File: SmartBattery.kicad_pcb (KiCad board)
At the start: 2 copper layers, 168 parts, among them J1 USB_C_Receptacle_USB2.0, J10 Conn_01x02, J11 Conn_01x02, J2 ST-USB-003A, J3 RJ45_LED_Shielded, J4 Conn_01x02, J5 Conn_01x02, J6 Conn_01x02, J7 Conn_01x02, J8 Conn_01x02, J9 Conn_01x02, Q1 AO4407A, Q10 AO4468, Q11 AO4468, Q2 2n7002K, Q3 AO4468, Q4 AO4468, Q5 AO4468, Q6 AO4468, Q7 2n7002K, Q8 AO4468, Q9 AO4468, SW1 SW_Push, SW2 SW_Push, U1 bq2477x, U2 BQ294706DSGR, U3 ITV4030, U4 BQ40Z50

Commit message: Adding lots of changes. Started output Stage
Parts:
- removed Q3, Q5: AO4468, Package_TO_SOT_SMD:TDSON-8-1
- added L2: MWSA0603-2R2MT, SmartBattery:MWSA0603, F.Cu at (16.2, 17.6)
- added U5: LM5175PWPR, SmartBattery:IC_TPS61196PWPRQ1, F.Cu at (8.07, 20.2)
- J10, J11, J4, J5, J6, J7, J8, J9: value Conn_01x02 -> JST 2P-1.0; footprint Connector_JST:JST_PH_S2B-PH-K_1x02_P2.00mm_Horizontal -> Connector_JST:JST_SH_SM02B-SRSS-TB_1x02-1MP_P1.00mm_Horizontal
- J3: value RJ45_LED_Shielded -> Barrel_Jack_MountingPin; footprint Connector_RJ:RJ45_Amphenol_RJHSE538X -> Connector_BarrelJack:BarrelJack_Horizontal
- Q10, Q11, Q4, Q6, Q8, Q9: footprint Package_TO_SOT_SMD:TDSON-8-1 -> SmartBattery:SOIC-8_Alpha_Omega
- TP18: moved to B.Cu
- moved J2 140.8 mm to (7.45, 4.47), turned to 90 degrees
- moved J1 122.3 mm to (21.8, 5.89), turned to 180 degrees
- moved D2 108.7 mm to (12.0, 52.9)
- moved D3 108.7 mm to (6.61, 52.8)
- moved D4 108.7 mm to (33.8, 53.1)
- moved D6 108.7 mm to (38.6, 53.1)
- moved D7 108.7 mm to (21.6, 52.9)
- moved J3 106.8 mm to (91.0, 11.4), turned to 180 degrees
- moved C16 104.5 mm to (75.0, 21.4)
- moved C17 104.5 mm to (65.1, 21.4)
- moved TP1 81.3 mm to (46.7, 34.4)
- moved C1 81.3 mm to (37.7, 16.0)
- moved C52 81.3 mm to (42.6, 16.0)
- moved C9 81.3 mm to (43.2, 36.6)
- moved R38 81.3 mm to (52.3, 34.2)
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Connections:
- C52 pad 1: /Charger/BATT_PACK_P -> /Battery connection and protection/BATT_PACK_P
- D9 pad 2: /Charger/BATT_PACK_P -> /Battery connection and protection/BATT_PACK_P
- J10 pad 1: Net-(F4-Pad1) -> BAT_VN_3
- J10 pad 2: BAT_VN_0 -> Net-(F5-Pad1)
- J11 pad 1: Net-(F8-Pad1) -> BAT_VN_3
- J11 pad 2: BAT_VN_0 -> Net-(F1-Pad1)
- J3 pad 3: Net-(J3-Pad3) -> (no net)
- J4 pad 1: Net-(F1-Pad1) -> BAT_VN_0
- J4 pad 2: BAT_VN_3 -> Net-(F8-Pad1)
- J5 pad 1: Net-(F5-Pad1) -> BAT_VN_0
- J5 pad 2: BAT_VN_3 -> Net-(F4-Pad1)
- J6 pad 1: Net-(F2-Pad1) -> BAT_VN_1
- J6 pad 2: BAT_VN_2 -> Net-(F7-Pad1)
- J7 pad 1: Net-(F6-Pad1) -> BAT_VN_1
- J7 pad 2: BAT_VN_2 -> Net-(F3-Pad1)
- J8 pad 1: Net-(F3-Pad1) -> BAT_VN_2
- J8 pad 2: BAT_VN_1 -> Net-(F6-Pad1)
- J9 pad 1: Net-(F7-Pad1) -> BAT_VN_2
- J9 pad 2: BAT_VN_1 -> Net-(F2-Pad1)
- Q1 pad 5: /Charger/BATT_PACK_P -> /Battery connection and protection/BATT_PACK_P
- Q1 pad 6: /Charger/BATT_PACK_P -> /Battery connection and protection/BATT_PACK_P
- Q1 pad 7: /Charger/BATT_PACK_P -> /Battery connection and protection/BATT_PACK_P
- Q1 pad 8: /Charger/BATT_PACK_P -> /Battery connection and protection/BATT_PACK_P
- Q10 pad 1: Net-(Q10-Pad1) -> Net-(C51-Pad1)
- Q10 pad 3: Net-(C39-Pad2) -> Net-(C51-Pad1)
- Q10 pad 4: (no net) -> Net-(Q10-Pad4)
- Q10 pad 5: (no net) -> Net-(C39-Pad2)
- Q11 pad 1: Net-(Q11-Pad1) -> GND
- Q11 pad 2: Net-(Q11-Pad2) -> GND
- Q11 pad 3: Net-(C51-Pad1) -> GND
- Q11 pad 4: (no net) -> Net-(Q11-Pad4)
- Q11 pad 5: (no net) -> Net-(C51-Pad1)
- Q4 pad 1: Net-(Q3-Pad1) -> Net-(C30-Pad2)
- Q4 pad 3: Net-(Q3-Pad3) -> Net-(C30-Pad2)
- Q4 pad 4: (no net) -> Net-(Q4-Pad4)
- Q4 pad 5: (no net) -> Net-(Q4-Pad5)
- Q6 pad 1: Net-(Q5-Pad1) -> /Battery connection and protection/BATT_PACK_P
- Q6 pad 3: Net-(Q3-Pad3) -> /Battery connection and protection/BATT_PACK_P
- Q6 pad 4: (no net) -> Net-(Q6-Pad4)
- Q6 pad 5: (no net) -> Net-(Q4-Pad5)
- Q7 pad 3: Net-(Q5-Pad1) -> Net-(Q6-Pad4)
- Q8 pad 1: Net-(Q8-Pad1) -> Net-(C47-Pad1)
- Q8 pad 3: /Charger/ADAPTER_IN -> Net-(C47-Pad1)
- Q8 pad 4: (no net) -> Net-(Q8-Pad4)
- Q8 pad 5: (no net) -> /Charger/ADAPTER_IN
- Q9 pad 1: Net-(Q8-Pad1) -> Net-(C47-Pad1)
- Q9 pad 3: Net-(C37-Pad2) -> Net-(C47-Pad1)
- Q9 pad 4: (no net) -> Net-(Q8-Pad4)
- Q9 pad 5: (no net) -> Net-(C37-Pad2)
- R18 pad 1: Net-(Q3-Pad1) -> Net-(Q4-Pad4)
- R22 pad 2: Net-(Q3-Pad1) -> Net-(Q4-Pad4)
- R26 pad 2: Net-(Q3-Pad3) -> Net-(Q4-Pad5)
- R27 pad 2: Net-(Q5-Pad1) -> Net-(Q6-Pad4)
- R29 pad 1: Net-(Q5-Pad1) -> Net-(Q6-Pad4)
- R42 pad 1: Net-(Q8-Pad1) -> Net-(Q8-Pad4)
- R46 pad 2: Net-(Q10-Pad1) -> Net-(Q10-Pad4)
- R47 pad 2: Net-(Q11-Pad1) -> Net-(Q11-Pad4)
- R48 pad 1: /Charger/BATT_PACK_P -> /Battery connection and protection/BATT_PACK_P
- TP11 pad 1: Net-(Q3-Pad1) -> Net-(Q4-Pad4)
- TP12 pad 1: Net-(Q3-Pad3) -> Net-(Q4-Pad5)
- TP14 pad 1: Net-(Q5-Pad1) -> Net-(Q6-Pad4)
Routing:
- added copper zone on F.Cu, net BAT_VN_0
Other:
- board outline added: 100 x 70 mm

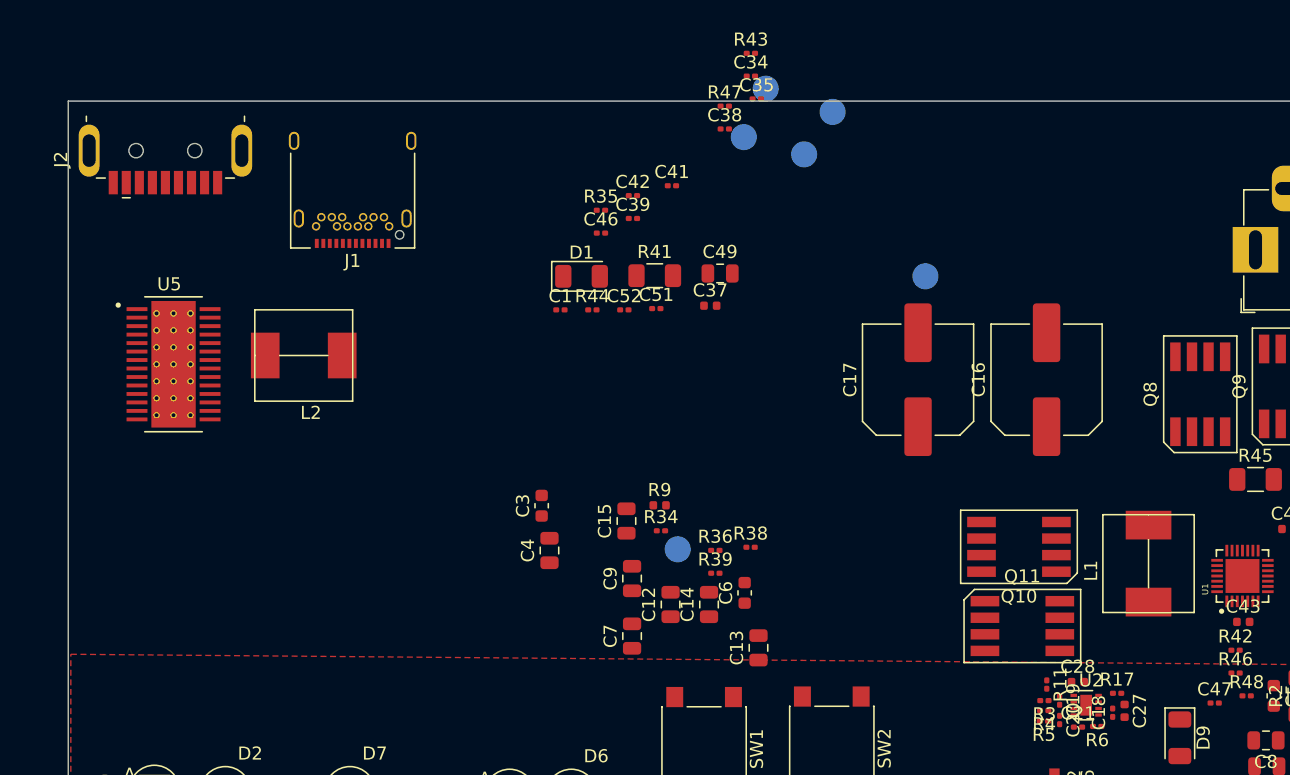
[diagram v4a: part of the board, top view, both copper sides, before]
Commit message: Lots of changes for MFG: parts info
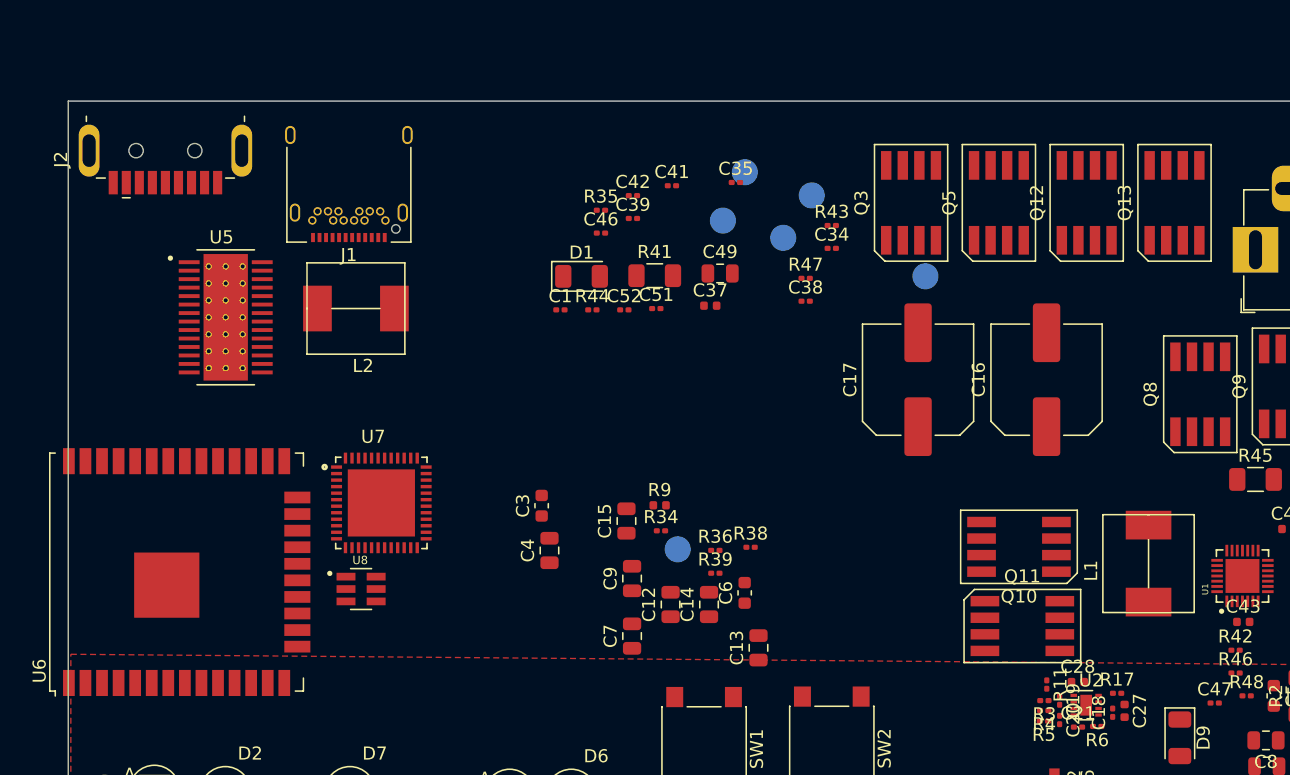
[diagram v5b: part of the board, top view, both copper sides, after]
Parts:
- added Q12: AO4468, SmartBattery:SOIC-8_Alpha_Omega, F.Cu at (78.1, 7.80)
- added Q13: AO4468, SmartBattery:SOIC-8_Alpha_Omega, F.Cu at (84.8, 7.80)
- added Q3: AO4468, SmartBattery:SOIC-8_Alpha_Omega, F.Cu at (64.6, 7.80)
- added Q5: AO4468, SmartBattery:SOIC-8_Alpha_Omega, F.Cu at (71.3, 7.80)
- added U6: ESP32-WROOM-32U, RF_Module:ESP32-WROOM-32U, F.Cu at (8.30, 36.1)
- added U7: ATSAMD21G18A-MU, SmartBattery:QFN50P700X700X90-49N, F.Cu at (24.0, 30.8)
- added U8: TPS54202HDDCR, SmartBattery:SOT95P280X110-6N, F.Cu at (22.4, 37.4)
- moved C38 14.6 mm to (56.5, 15.3)
- moved R47 14.6 mm to (56.5, 13.6)
- moved C34 14.6 mm to (58.5, 11.3)
- moved R43 14.6 mm to (58.5, 9.54)
- moved C35 6.60 mm to (51.2, 6.24)
- moved TP20 6.60 mm to (57.0, 7.23)
- moved TP22 6.60 mm to (51.9, 5.45)
- moved TP21 6.60 mm to (54.8, 10.5)
- moved TP19 6.60 mm to (50.2, 9.16)
- moved L2 5.38 mm to (20.2, 14.0)
- moved U5 5.38 mm to (12.1, 16.6)
- moved J1 0.54 mm to (21.5, 5.44)

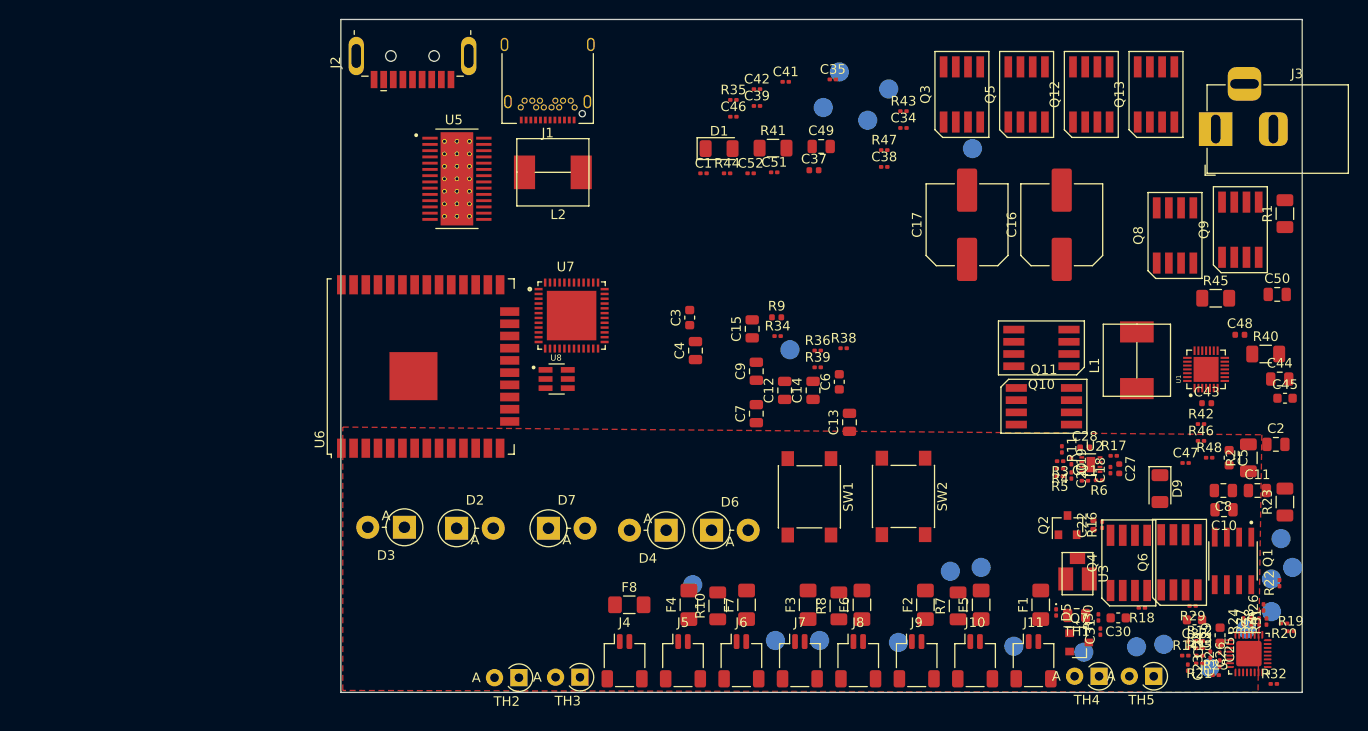
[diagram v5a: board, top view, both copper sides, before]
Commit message: Switching over to jlpcb
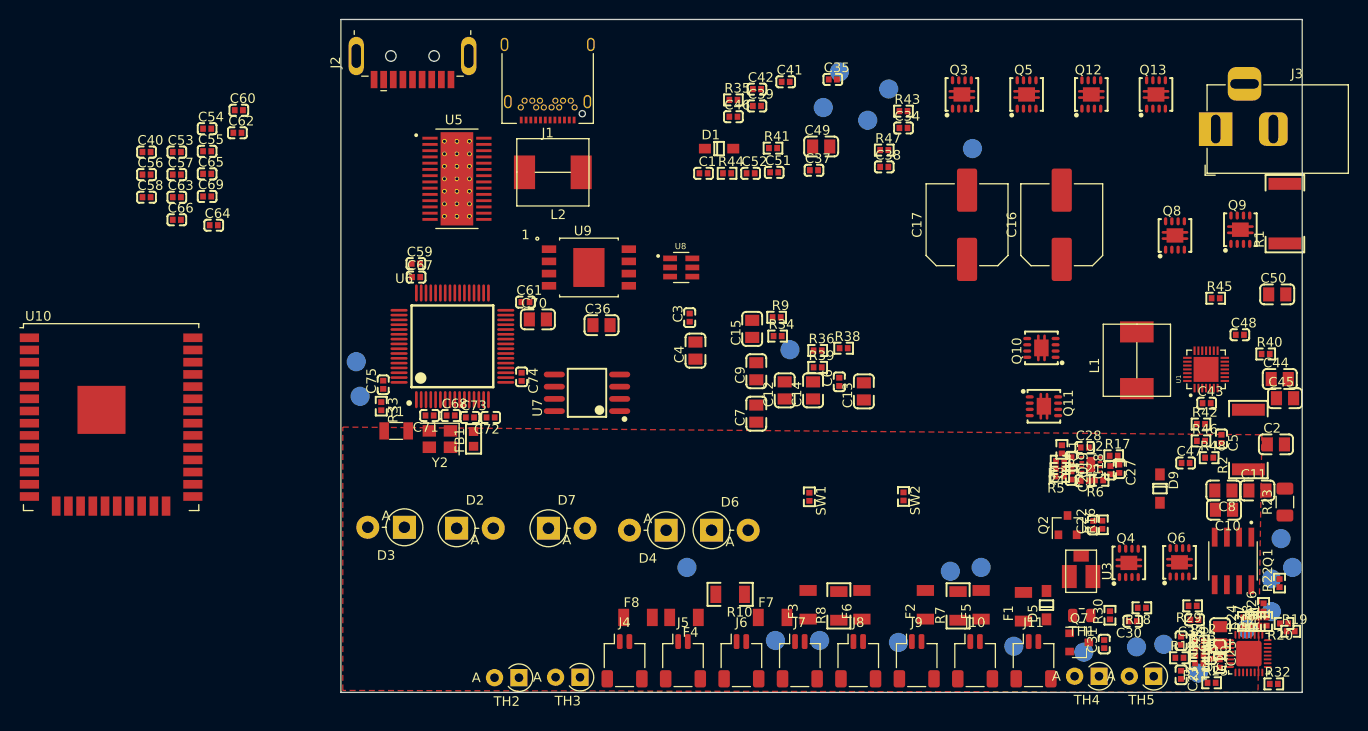
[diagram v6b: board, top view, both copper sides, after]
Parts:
- added C36: 2.2u 6.3v, lc_lib:0805_C, F.Cu at (27.1, 31.8)
- added C40: 0.1u 6.3v, lc_lib:0402_C, F.Cu at (-20.2, 13.8)
- added C53: 0.1u 6.3v, lc_lib:0402_C, F.Cu at (-17.1, 13.8)
- added C54: 0.1u 6.3v, lc_lib:0402_C, F.Cu at (-13.9, 11.4)
- added C55: 0.1u 6.3v, lc_lib:0402_C, F.Cu at (-13.9, 13.7)
- added C56: 0.1u 6.3v, lc_lib:0402_C, F.Cu at (-20.2, 16.1)
- added C57: 0.1u 6.3v, lc_lib:0402_C, F.Cu at (-17.1, 16.1)
- added C58: 15 pF 0402, lc_lib:0402_C, F.Cu at (-20.2, 18.5)
- added C59: 0.1u 6.3v, lc_lib:0402_C, F.Cu at (7.80, 25.4)
- added C60: 15 pF 0402, lc_lib:0402_C, F.Cu at (-10.6, 9.44)
- added C61: 0.1u 6.3v, lc_lib:0402_C, F.Cu at (19.2, 29.4)
- added C62: 0.1u 6.3v, lc_lib:0402_C, F.Cu at (-10.8, 11.8)
- added C63: 0.1u 6.3v, lc_lib:0402_C, F.Cu at (-17.1, 18.5)
- added C64: 0.1u 6.3v, lc_lib:0402_C, F.Cu at (-13.2, 21.4)
- added C65: 0.1u 6.3v, lc_lib:0402_C, F.Cu at (-13.9, 16.1)
- added C66: 0.1u 6.3v, lc_lib:0402_C, F.Cu at (-17.1, 20.8)
- added C67: 0.1u 6.3v, lc_lib:0402_C, F.Cu at (7.83, 26.8)
- added C68: 12pF 0402, lc_lib:0402_C, F.Cu at (11.4, 41.2)
- added C69: 0.1u 6.3v, lc_lib:0402_C, F.Cu at (-13.9, 18.4)
- added C70: 2.2u 6.3v, lc_lib:0805_C, F.Cu at (20.5, 31.2)
- added C71: 12pF 0402, lc_lib:0402_C, F.Cu at (9.22, 41.2)
- added C72: 0.1u 6.3v, lc_lib:0402_C, F.Cu at (15.6, 41.4)
- added C73: 0.1u 6.3v, lc_lib:0402_C, F.Cu at (13.4, 41.4)
- added C74: 0.1u 6.3v, lc_lib:0402_C, F.Cu at (18.8, 37.2)
- added C75: 0.1u 6.3v, lc_lib:0402_C, F.Cu at (4.40, 38.0)
- added FB1: Ferrite_Bead_Small, lc_lib:0603_L, F.Cu at (13.8, 43.6)
- added R33: 0, lc_lib:0402_R, F.Cu at (4.20, 40.2)
- added TP23: TestPoint, TestPoint:TestPoint_Pad_D2.0mm, B.Cu at (2.00, 39.2)
- added TP24: TestPoint, TestPoint:TestPoint_Pad_D2.0mm, B.Cu at (1.60, 35.6)
- added U10: ESP32-WROOM-32U, RF_Module:ESP32-WROOM-32U, F.Cu at (-23.9, 41.4)
- added U9: FS35ND01G-S1Y2QWFI000, SmartBattery:WSON8_8x6mm, F.Cu at (25.8, 25.8)
- added Y1: Q13FC1350000400, Crystal:Crystal_SMD_3215-2Pin_3.2x1.5mm, F.Cu at (5.75, 42.8)
- added Y2: Crystal_GND24, Crystal:Crystal_SMD_3225-4Pin_3.2x2.5mm, F.Cu at (10.3, 43.6)
- C1: value 1uF 16v -> 1uF; footprint Capacitor_SMD:C_0201_0603Metric -> lc_lib:0402_C
- C10, C11, C12, C13, C14, C15, C2, C4, C44, C49, C50, C7, C8, C9: footprint Capacitor_SMD:C_0805_2012Metric -> lc_lib:0805_C
- C18, C19, C20, C21, C23, C24, C25, C26, C31, C32, C34, C35, C38, C39, C41, C42, C46, C47, C51, C52: footprint Capacitor_SMD:C_0201_0603Metric -> lc_lib:0402_C
- C22, C27, C28, C37, C43, C48: footprint Capacitor_SMD:C_0402_1005Metric -> lc_lib:0402_C
- C29, C45: footprint Capacitor_SMD:C_0603_1608Metric -> lc_lib:0805_C
- C3, C6: value 0.1u -> 0.1u 25v; footprint Capacitor_SMD:C_0603_1608Metric -> lc_lib:0402_C
- C30, C33, C5: footprint Capacitor_SMD:C_0603_1608Metric -> lc_lib:0402_C
- D1, D9: footprint Diode_SMD:D_1206_3216Metric -> lc_lib:SOD-123
- D5: footprint Diode_SMD:D_0201_0603Metric -> lc_lib:SOD-123
- F1, F2, F3, F4, F5, F6, F7, F8: footprint Fuse:Fuse_1206_3216Metric_Pad1.42x1.75mm_HandSolder -> lc_lib:1206
- Q10, Q11, Q12, Q13, Q3, Q4, Q5, Q6, Q8, Q9: value AO4468 -> AON7400A; footprint SmartBattery:SOIC-8_Alpha_Omega -> lc_lib:QFN-8_3X3X065P
- R1, R2: footprint Resistor_SMD:R_1206_3216Metric -> lc_lib:2512_R
- R10, R7, R8: footprint Resistor_SMD:R_1206_3216Metric -> lc_lib:1206_R
- R11, R12, R13, R14, R15, R16, R17, R18, R19, R20, R21, R22, R24, R25, R26, R27, R28, R29, R3, R30, R31, R32, R34, R35, R36, R38, R39, R4, R42, R43, R44, R46, R47, R48, R5, R6: footprint Resistor_SMD:R_0201_0603Metric -> lc_lib:0402_R
- R40, R41, R45: footprint Resistor_SMD:R_1206_3216Metric -> lc_lib:0402_R
- R9: footprint Resistor_SMD:R_0402_1005Metric -> lc_lib:0402_R
- SW1, SW2: footprint Button_Switch_SMD:SW_Push_1P1T_NO_6x6mm_H9.5mm -> lc_lib:0402_R
- U6: value ESP32-WROOM-32U -> STM32F730R8T6; footprint RF_Module:ESP32-WROOM-32U -> lc_lib:TQFP-64_10X10X05P
- U7: value ATSAMD21G18A-MU -> W25Q128JVSIQ; footprint SmartBattery:QFN50P700X700X90-49N -> lc_lib:SOP-8_208MIL
- moved U8 17.4 mm to (35.4, 25.8)
- moved U7 8.19 mm to (25.6, 38.8), turned to 90 degrees
- moved U6 3.91 mm to (11.6, 34.0), turned to 0 degrees
- moved C13 3.55 mm to (54.4, 38.7)
- moved F7 3.01 mm to (44.9, 62.2), turned to 0 degrees
- moved C5 2.12 mm to (91.6, 43.6)
- moved R2 1.90 mm to (94.4, 43.7)
- moved TP9 1.90 mm to (36.0, 57.0)
- moved F1 1.81 mm to (71.0, 61.1)
- moved R10 1.76 mm to (40.5, 59.8), turned to 180 degrees
- moved F8 1.60 mm to (30.9, 62.2)
- moved C30 1.55 mm to (82.4, 62.6)
- moved F4 1.41 mm to (35.7, 62.2), turned to 180 degrees
- moved C31 1.36 mm to (79.4, 65.0)
- moved TP14 1.31 mm to (89.2, 68.0)
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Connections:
- U6 pad 1: Net-(U6-Pad1) -> Net-(R33-Pad2)
- U6 pad 12: Net-(U6-Pad12) -> GND
- U6 pad 15: Net-(U6-Pad1) -> Net-(U6-Pad15)
- U6 pad 18: Net-(U6-Pad18) -> GND
- U6 pad 19: Net-(U6-Pad19) -> /MCU/Power_3p3v
- U6 pad 31: Net-(U6-Pad31) -> GND
- U6 pad 32: Net-(U6-Pad32) -> /MCU/Power_3p3v
- U6 pad 38: Net-(U6-Pad1) -> Net-(U6-Pad38)
- U6 pad 39: (no net) -> Net-(U6-Pad39)
- U7 pad 4: Net-(U7-Pad4) -> GND
- U7 pad 8: Net-(U7-Pad8) -> /MCU/Power_3p3v
